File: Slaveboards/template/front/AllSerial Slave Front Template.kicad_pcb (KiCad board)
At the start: 2 copper layers, 71.5 x 24 mm, 2 parts

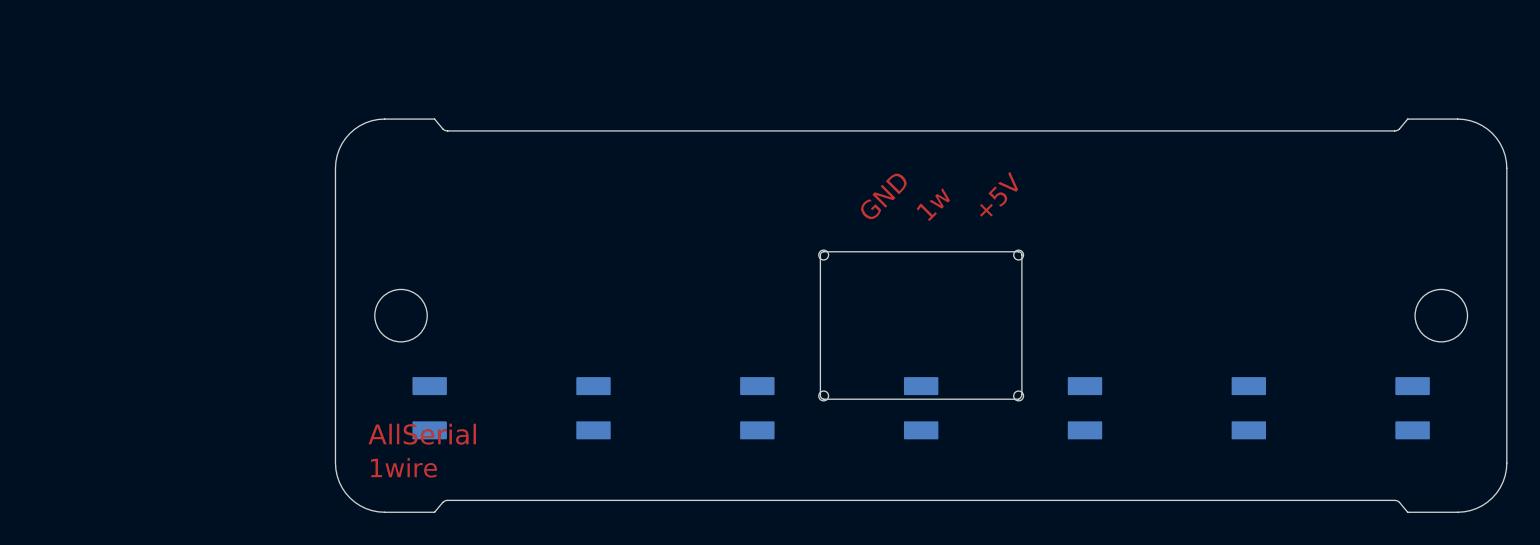
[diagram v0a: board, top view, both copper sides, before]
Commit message: Update AllSerial libraries
update projects
add slave project template
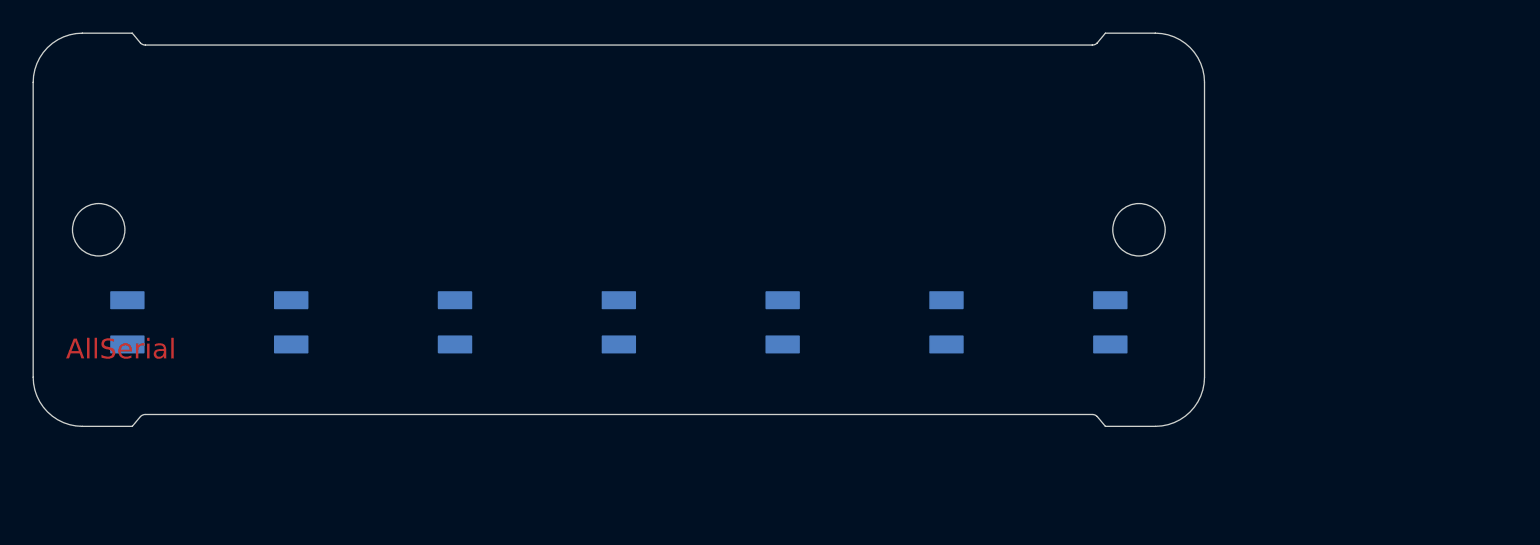
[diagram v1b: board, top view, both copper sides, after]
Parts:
- removed E$2: , AllSerial_Front:Frontpanel_2_Holes
- E$1: value (none) -> Val**; footprint AllSerial_Front:Metz_PT11303HBBN_182 -> AllSerial Front:Frontpanel_2_Holes
- moved E$1 19.2 mm to (130.0, 111.8)
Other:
- outline, holes or cut-outs redrawn
- board text removed: "+5V"
- board text removed: "1w"
- board text removed: "1wire"
- board text removed: "AllSerial 1wire front 26/23"
- board text removed: "GND"
